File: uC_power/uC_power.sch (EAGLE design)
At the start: 45 parts, among them SW1 TOGURUSUIITI

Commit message: Add files via upload
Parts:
- added C10: (no value), rcl:C-EUC1608
- added JP1, JP2: (no value), pinhead:PINHD-1X2
- added R16: 10k, user_rcl:R_REG
- added R_I3: (no value), user_rcl:R_SHUGOU2
- added TRIM_R3: 50k, user_rcl:R_TRIM2
- R11, R8: value 20k -> 10k
- R13: value 10k -> 470k
- TRIM_R1, TRIM_R2: value 10k -> 22k
- U$9: value SSOT6_FET -> NJM2380; device user_tr_fet_igbt:SSOT6_FET -> user_ic:NJM2380
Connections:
- removed net N$17: R13.1, U$9.PIN1_G1, U$9.PIN4_D2
- removed net N$20: SW1.2, SW1.C, U$9.PIN6_D1
- new net N$19: C6.1, IC3.11_IN4+, IC3.8_IN3-, JP2.1, R6.1, TRIM_R2.E, U$2.PIN4_C
- new net N$25: IC3.10_IN4-, IC3.5_IN1+, IC3.5_IN2-, IC3.9_IN3+, R_I3.5, R_I3.8
- new net V_SENS: C7.1, GYAKUSETU_FET.1_S2, GYAKUSETU_FET.3_S1, IC3.3_V+, R10.2, R12.2, R5.2, R6.2, R7.1, R9.2, R_I1.5, R_I1.6, R_I1.7, R_I1.8, R_I3.1, SW_FET.1_S2, SW_FET.3_S1, TRIM_R3.E
- net COMP4: no longer U$9.PIN3_G2
- net GND: now also C10.2, JP1.2, JP2.2, R16.1, R_I3.4, U$9.PIN2_A; no longer U$9.PIN2_S2, U$9.PIN5_S1
- net N$5: now also JP1.1
- net N$6: now also C10.1, SW1.2, SW1.C, U$9.PIN4_C; no longer C6.1, IC3.11_IN4+, IC3.8_IN3-, R6.2, TRIM_R2.E, U$2.PIN4_C
- net N$8: now also R13.1, R16.2, TRIM_R3.A, TRIM_R3.S, U$9.PIN5_REF; no longer C7.1, GYAKUSETU_FET.1_S2, GYAKUSETU_FET.3_S1, IC3.10_IN4-, IC3.3_V+, IC3.5_IN1+, IC3.5_IN2-, IC3.9_IN3+, R10.2, R12.2, R13.2, R5.2, R6.1, R7.1, R9.2, R_I1.5, R_I1.6, R_I1.7, R_I1.8, SW_FET.1_S2, SW_FET.3_S1
- net V12: now also R13.2
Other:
- note added: "37kに設定"
- note added: "5,75Vに設定"
- note added: "5.5Vに設定"
- moved on the sheet: C1, C2, C3, C4, C5, C6, C7, C8, C9, GYAKUSETU_FET, IC1, IC3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

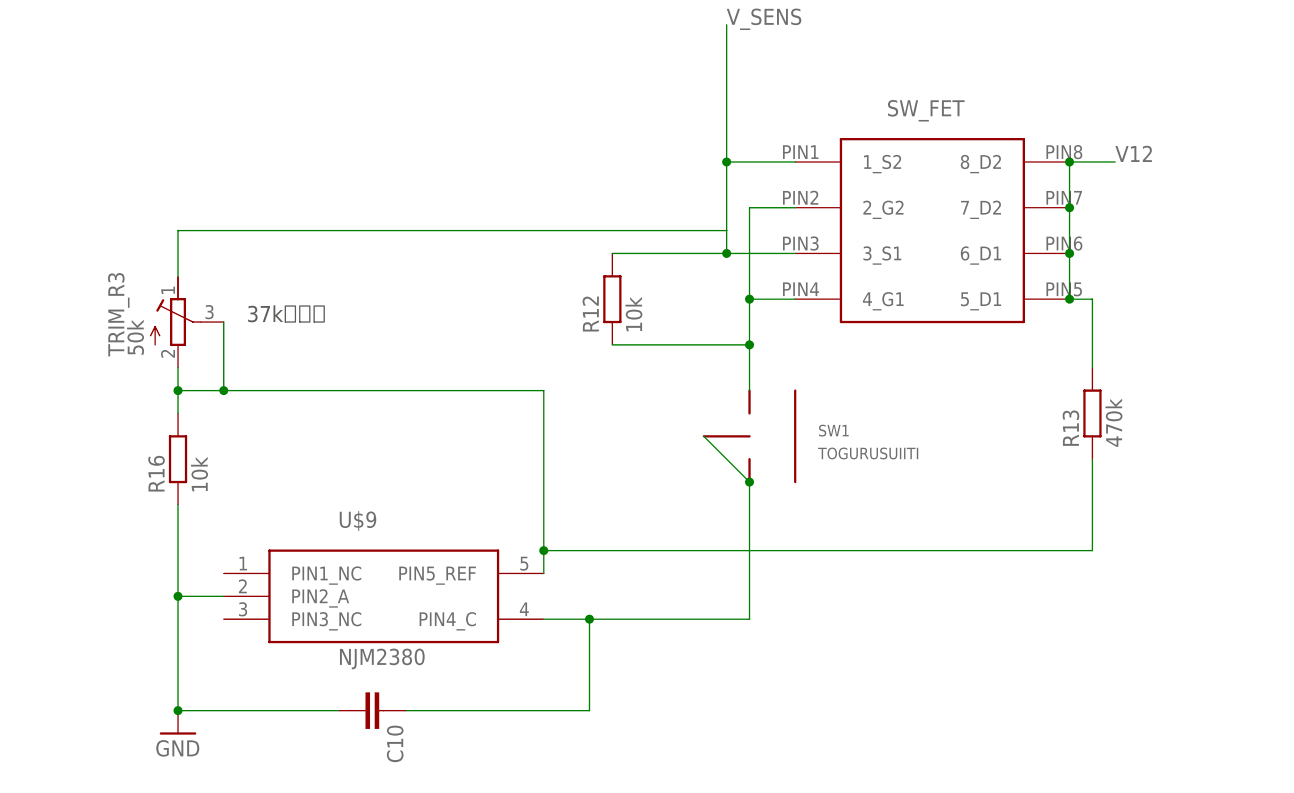
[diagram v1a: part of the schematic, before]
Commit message: uvloを取っ払った
uvloを付けたのはいいけど調節がめんどくさいことに気が付いた
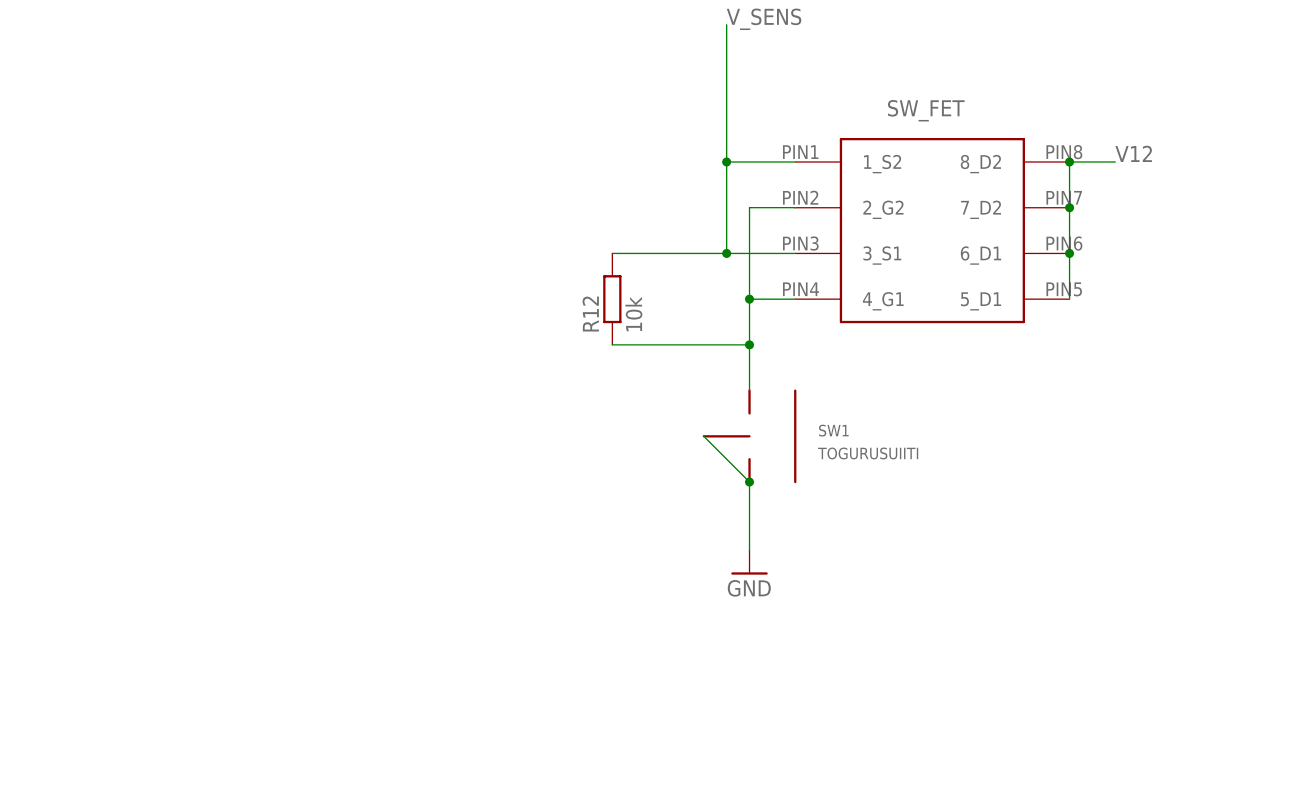
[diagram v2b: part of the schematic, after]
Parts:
- removed C10: (no value), rcl:C-EUC1608
- removed R13: 470k, user_rcl:R_REG
- removed R16: 10k, user_rcl:R_REG
- removed TRIM_R3: 50k, user_rcl:R_TRIM2
- removed U$9: NJM2380, user_ic:NJM2380
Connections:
- removed net N$6: C10.1, SW1.2, SW1.C, U$9.PIN4_C
- removed net N$8: R13.1, R16.2, TRIM_R3.A, TRIM_R3.S, U$9.PIN5_REF
- net GND: now also SW1.2, SW1.C; no longer C10.2, R16.1, U$9.PIN2_A
- net V12: no longer R13.2
- net V_SENS: no longer TRIM_R3.E
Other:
- note removed: "37kに設定"
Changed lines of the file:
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@@
 <part name="LED2" library="user_leds" deviceset="1608LED" device=""/>
 <part name="SW1" library="user_swich" deviceset="TOGURUSUIITI" device=""/>
-<part name="R13" library="user_rcl" deviceset="R_REG" device="" value="470k"/>
 <part name="R_I3" library="user_rcl" deviceset="R_SHUGOU" device="2"/>
 <part name="GND10" library="supply1" library_urn="urn:adsk.eagle:library:371" deviceset="GND" device=""/>
 <part name="R6" library="user_rcl" deviceset="R_REG" device="" value="10k"/>
-<part name="U$9" library="user_ic" deviceset="NJM2380" device=""/>
-<part name="GND11" library="supply1" library_urn="urn:adsk.eagle:library:371" deviceset="GND" device=""/>
-<part name="R16" library="user_rcl" deviceset="R_REG" device="" value="10k"/>
-<part name="C10" library="rcl" library_urn="urn:adsk.eagle:library:334" deviceset="C-EU" device="C1608" package3d_urn="urn:adsk.eagle:package:23621/2"/>
-<part name="TRIM_R3" library="user_rcl" deviceset="R_TRIM" device="2" value="50k"/>
 <part name="JP1" library="pinhead" library_urn="urn:adsk.eagle:library:325" deviceset="PINHD-1X2" device="" package3d_urn="urn:adsk.eagle:package:22435/2"/>
 <part name="JP2" library="pinhead" library_urn="urn:adsk.eagle:library:325" deviceset="PINHD-1X2" device="" package3d_urn="urn:adsk.eagle:package:22435/2"/>
+<part name="GND7" library="supply1" library_urn="urn:adsk.eagle:library:371" deviceset="GND" device=""/>
 </parts>
 <sheets>
 <sheet>
 <plain>
-<text x="12.7" y="50.8" size="1.778" layer="97">37kに設定</text>
 <text x="99.06" y="116.84" size="1.778" layer="97">5.5Vに設定</text>
 <text x="99.06" y="139.7" size="1.778" layer="97">5,75Vに設定</text>
@@
 <attribute name="VALUE" x="76.2" y="35.56" size="1.27" layer="96"/>
 </instance>
-<instance part="R13" gate="G$1" x="106.68" y="40.64" smashed="yes" rot="R90">
-<attribute name="NAME" x="105.1814" y="36.83" size="1.778" layer="95" rot="R90"/>
-<attribute name="VALUE" x="109.982" y="36.83" size="1.778" layer="96" rot="R90"/>
-</instance>
 <instance part="R_I3" gate="G$1" x="139.7" y="172.72" smashed="yes">
 <attribute name="NAME" x="137.795" y="177.8" size="1.778" layer="95"/>
@@
 <attribute name="VALUE" x="120.142" y="189.23" size="1.778" layer="96" rot="R90"/>
 </instance>
-<instance part="U$9" gate="G$1" x="27.94" y="20.32" smashed="yes">
-<attribute name="NAME" x="22.86" y="27.94" size="1.778" layer="95"/>
-<attribute name="VALUE" x="22.86" y="12.7" size="1.778" layer="96"/>
-</instance>
-<instance part="GND11" gate="1" x="5.08" y="5.08" smashed="yes">
-<attribute name="VALUE" x="2.54" y="2.54" size="1.778" layer="96"/>
-</instance>
-<instance part="R16" gate="G$1" x="5.08" y="35.56" smashed="yes" rot="R90">
-<attribute name="NAME" x="3.5814" y="31.75" size="1.778" layer="95" rot="R90"/>
-<attribute name="VALUE" x="8.382" y="31.75" size="1.778" layer="96" rot="R90"/>
-</instance>
-<instance part="C10" gate="G$1" x="27.94" y="7.62" smashed="yes" rot="R270">
-<attribute name="NAME" x="28.321" y="6.096" size="1.778" layer="95" rot="R270"/>
-<attribute name="VALUE" x="23.241" y="6.096" size="1.778" layer="96" rot="R270"/>
-</instance>
-<instance part="TRIM_R3" gate="G$1" x="5.08" y="50.8" smashed="yes">
-<attribute name="NAME" x="-0.889" y="46.99" size="1.778" layer="95" rot="R90"/>
-<attribute name="VALUE" x="1.27" y="46.99" size="1.778" layer="96" rot="R90"/>
-</instance>
 <instance part="JP1" gate="G$1" x="86.36" y="111.76" smashed="yes" rot="R270">
 <attribute name="NAME" x="92.075" y="118.11" size="1.778" layer="95" rot="R270"/>
@@
 <attribute name="NAME" x="92.075" y="107.95" size="1.778" layer="95" rot="R270"/>
 <attribute name="VALUE" x="81.28" y="107.95" size="1.778" layer="96" rot="R270"/>
+</instance>
+<instance part="GND7" gate="1" x="68.58" y="22.86" smashed="yes">
+<attribute name="VALUE" x="66.04" y="20.32" size="1.778" layer="96"/>
 </instance>
 </instances>
@@
 </segment>
 <segment>
-<pinref part="GND11" gate="1" pin="GND"/>
-<pinref part="C10" gate="G$1" pin="2"/>
-<wire x1="22.86" y1="7.62" x2="5.08" y2="7.62" width="0.1524" layer="91"/>
-<pinref part="R16" gate="G$1" pin="1"/>
-<wire x1="5.08" y1="30.48" x2="5.08" y2="20.32" width="0.1524" layer="91"/>
-<junction x="5.08" y="7.62"/>
-<pinref part="U$9" gate="G$1" pin="PIN2_A"/>
-<wire x1="5.08" y1="20.32" x2="5.08" y2="7.62" width="0.1524" layer="91"/>
-<wire x1="10.16" y1="20.32" x2="5.08" y2="20.32" width="0.1524" layer="91"/>
-<junction x="5.08" y="20.32"/>
+<pinref part="SW1" gate="G$1" pin="C"/>
+<pinref part="SW1" gate="G$1" pin="2"/>
+<wire x1="68.58" y1="33.02" x2="63.5" y2="38.1" width="0.1524" layer="91"/>
+<junction x="68.58" y="33.02"/>
+<wire x1="68.58" y1="25.4" x2="68.58" y2="33.02" width="0.1524" layer="91"/>
+<pinref part="GND7" gate="1" pin="GND"/>
 </segment>
 </net>
@@
 <junction x="104.14" y="68.58"/>
 <label x="109.22" y="68.58" size="1.778" layer="95"/>
-<wire x1="104.14" y1="53.34" x2="106.68" y2="53.34" width="0.1524" layer="91"/>
-<junction x="104.14" y="53.34"/>
-<pinref part="R13" gate="G$1" pin="2"/>
-<wire x1="106.68" y1="53.34" x2="106.68" y2="45.72" width="0.1524" layer="91"/>
 </segment>
 <segment>
@@
 <pinref part="SW_FET" gate="G$1" pin="3_S1"/>
 <wire x1="73.66" y1="58.42" x2="66.04" y2="58.42" width="0.1524" layer="91"/>
-<wire x1="66.04" y1="58.42" x2="66.04" y2="60.96" width="0.1524" layer="91"/>
 <pinref part="SW_FET" gate="G$1" pin="1_S2"/>
-<wire x1="66.04" y1="60.96" x2="66.04" y2="68.58" width="0.1524" layer="91"/>
+<wire x1="66.04" y1="58.42" x2="66.04" y2="68.58" width="0.1524" layer="91"/>
 <wire x1="66.04" y1="68.58" x2="73.66" y2="68.58" width="0.1524" layer="91"/>
 <wire x1="66.04" y1="68.58" x2="66.04" y2="83.82" width="0.1524" layer="91"/>
@@
 <junction x="66.04" y="58.42"/>
 <label x="66.04" y="83.82" size="1.778" layer="95"/>
-<wire x1="5.08" y1="55.88" x2="5.08" y2="60.96" width="0.1524" layer="91"/>
-<wire x1="5.08" y1="60.96" x2="66.04" y2="60.96" width="0.1524" layer="91"/>
-<pinref part="TRIM_R3" gate="G$1" pin="E"/>
 </segment>
 <segment>
@@
 </segment>
 </net>
-<net name="N$6" class="0">
-<segment>
-<pinref part="SW1" gate="G$1" pin="C"/>
-<pinref part="SW1" gate="G$1" pin="2"/>
-<wire x1="68.58" y1="33.02" x2="63.5" y2="38.1" width="0.1524" layer="91"/>
-<junction x="68.58" y="33.02"/>
-<pinref part="U$9" gate="G$1" pin="PIN4_C"/>
-<wire x1="45.72" y1="17.78" x2="50.8" y2="17.78" width="0.1524" layer="91"/>
-<wire x1="50.8" y1="17.78" x2="68.58" y2="17.78" width="0.1524" layer="91"/>
-<wire x1="68.58" y1="17.78" x2="68.58" y2="33.02" width="0.1524" layer="91"/>
-<pinref part="C10" gate="G$1" pin="1"/>
-<wire x1="30.48" y1="7.62" x2="50.8" y2="7.62" width="0.1524" layer="91"/>
-<wire x1="50.8" y1="7.62" x2="50.8" y2="17.78" width="0.1524" layer="91"/>
-<junction x="50.8" y="17.78"/>
-</segment>
-</net>
-<net name="N$8" class="0">
-<segment>
-<pinref part="R13" gate="G$1" pin="1"/>
-<wire x1="106.68" y1="35.56" x2="106.68" y2="25.4" width="0.1524" layer="91"/>
-<pinref part="R16" gate="G$1" pin="2"/>
-<wire x1="5.08" y1="40.64" x2="5.08" y2="43.18" width="0.1524" layer="91"/>
-<pinref part="U$9" gate="G$1" pin="PIN5_REF"/>
-<wire x1="5.08" y1="43.18" x2="5.08" y2="45.72" width="0.1524" layer="91"/>
-<junction x="5.08" y="43.18"/>
-<wire x1="5.08" y1="43.18" x2="10.16" y2="43.18" width="0.1524" layer="91"/>
-<wire x1="10.16" y1="43.18" x2="45.72" y2="43.18" width="0.1524" layer="91"/>
-<wire x1="45.72" y1="43.18" x2="45.72" y2="25.4" width="0.1524" layer="91"/>
-<wire x1="45.72" y1="25.4" x2="45.72" y2="22.86" width="0.1524" layer="91"/>
-<wire x1="106.68" y1="25.4" x2="45.72" y2="25.4" width="0.1524" layer="91"/>
-<junction x="45.72" y="25.4"/>
-<pinref part="TRIM_R3" gate="G$1" pin="A"/>
-<pinref part="TRIM_R3" gate="G$1" pin="S"/>
-<wire x1="10.16" y1="50.8" x2="10.16" y2="43.18" width="0.1524" layer="91"/>
-<junction x="10.16" y="43.18"/>
-</segment>
-</net>

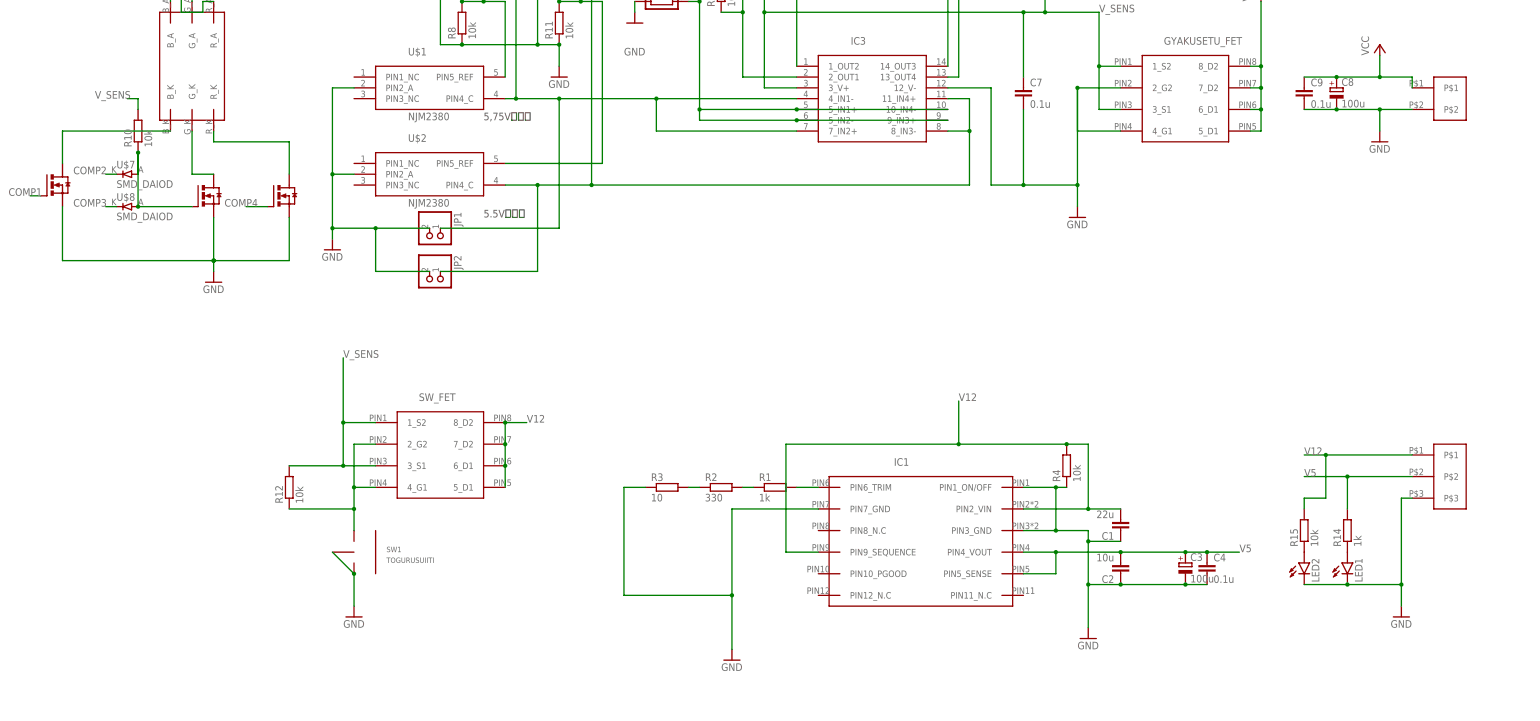
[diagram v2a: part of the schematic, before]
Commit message: UVLO、リセッタブルヒューズを追加
安全な自動シャットダウンのためのuvloを追加、ショート時の保護のためのリセッタブルヒューズを追加
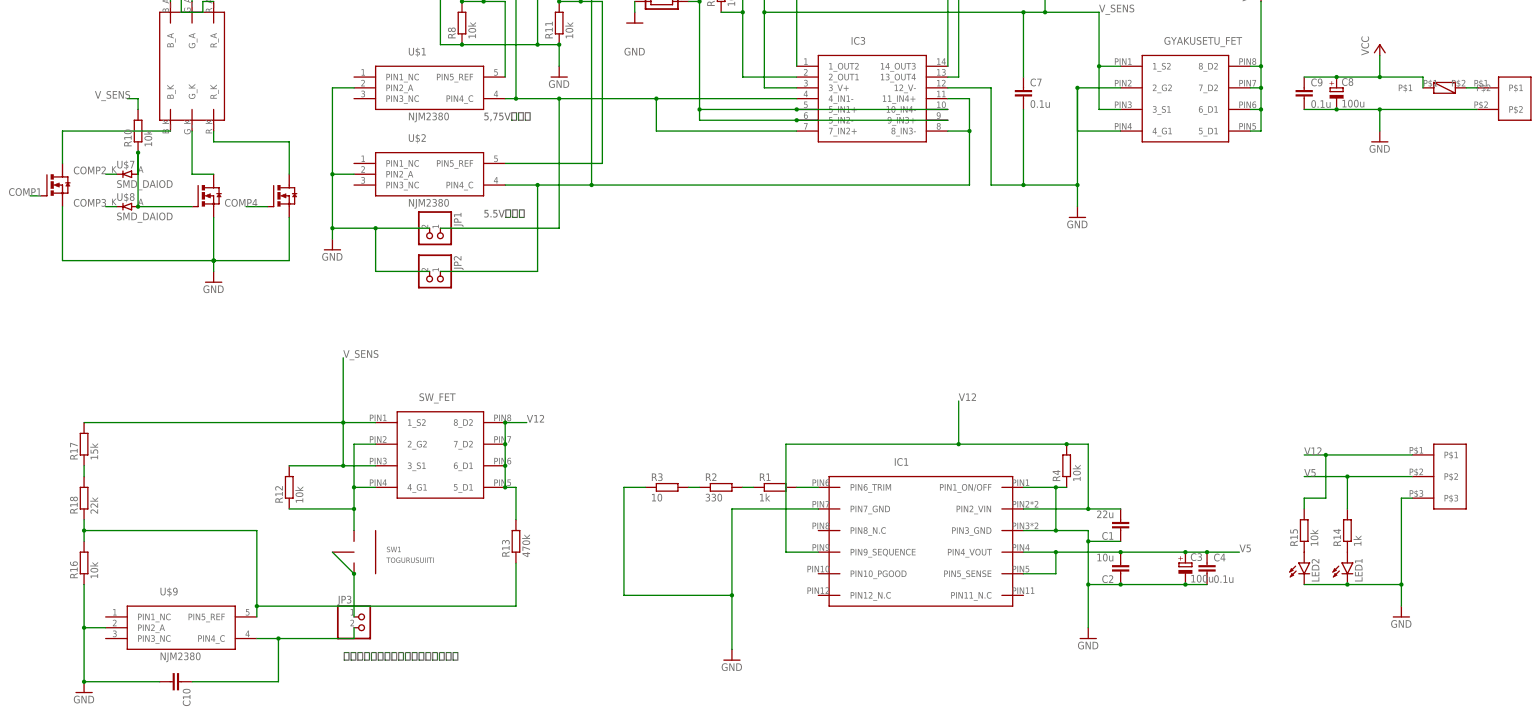
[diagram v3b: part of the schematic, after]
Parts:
- added C10: (no value), rcl:C-EUC1608
- added F1: (no value), user_hyuzu:RGEF300
- added JP3: (no value), pinhead:PINHD-1X2
- added R13: 470k, user_rcl:R_REG
- added R16: 10k, user_rcl:R_REG
- added R17: 15k, user_rcl:R_REG
- added R18: 22k, user_rcl:R_REG
- added U$9: NJM2380, user_ic:NJM2380
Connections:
- new net N$17: R17.1, R18.2
- new net N$20: JP3.1, SW1.2, SW1.C
- new net N$21: F1.P$2, U$11.P$1
- new net N$6: C10.1, JP3.2, U$9.PIN4_C
- new net N$8: R13.1, R16.2, R18.1, U$9.PIN5_REF
- net GND: now also C10.2, R16.1, U$9.PIN2_A; no longer SW1.2, SW1.C
- net V12: now also R13.2
- net VCC: now also F1.P$1; no longer U$11.P$1
- net V_SENS: now also R17.2
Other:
- note added: "緊急停止スイッチをつなぐピンヘッダ"
